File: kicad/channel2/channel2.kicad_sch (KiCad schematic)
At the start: 45 parts, among them J1 Conn_01x07_Male, J5V1 Conn_01x01_Male, Q1 BC846B, Q2 IRF3205, Q3 IRF3205, Q4 BC846B, Q5 IRF3205, Q6 IRF3205, U1 LM324

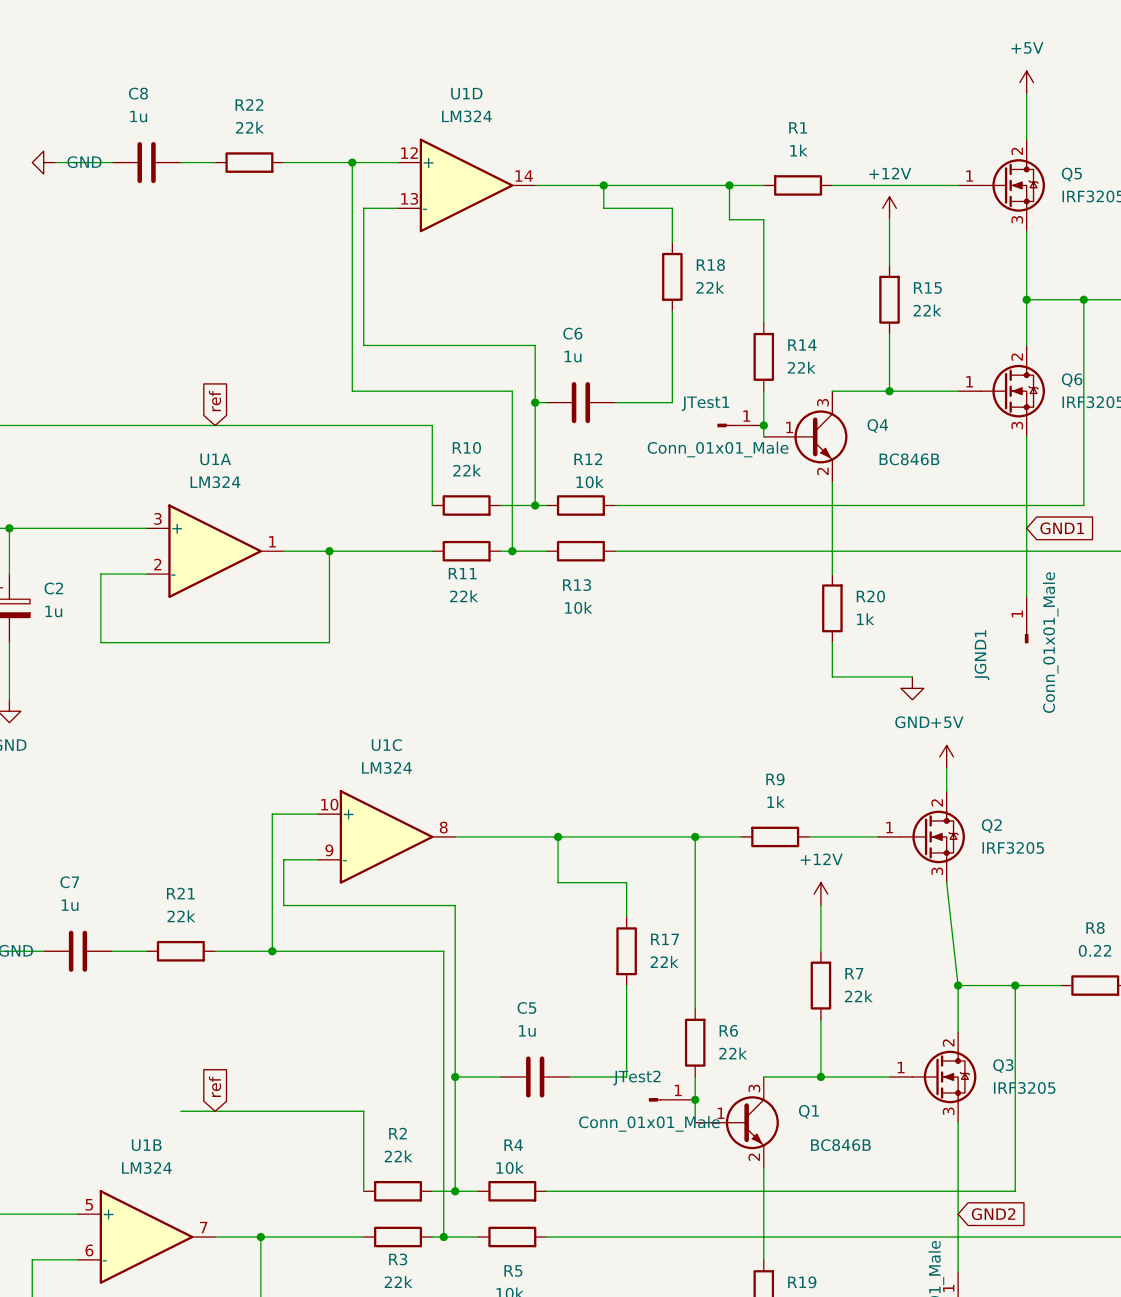
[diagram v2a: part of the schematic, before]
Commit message: minor schematic cleanups, improve opamp compensation
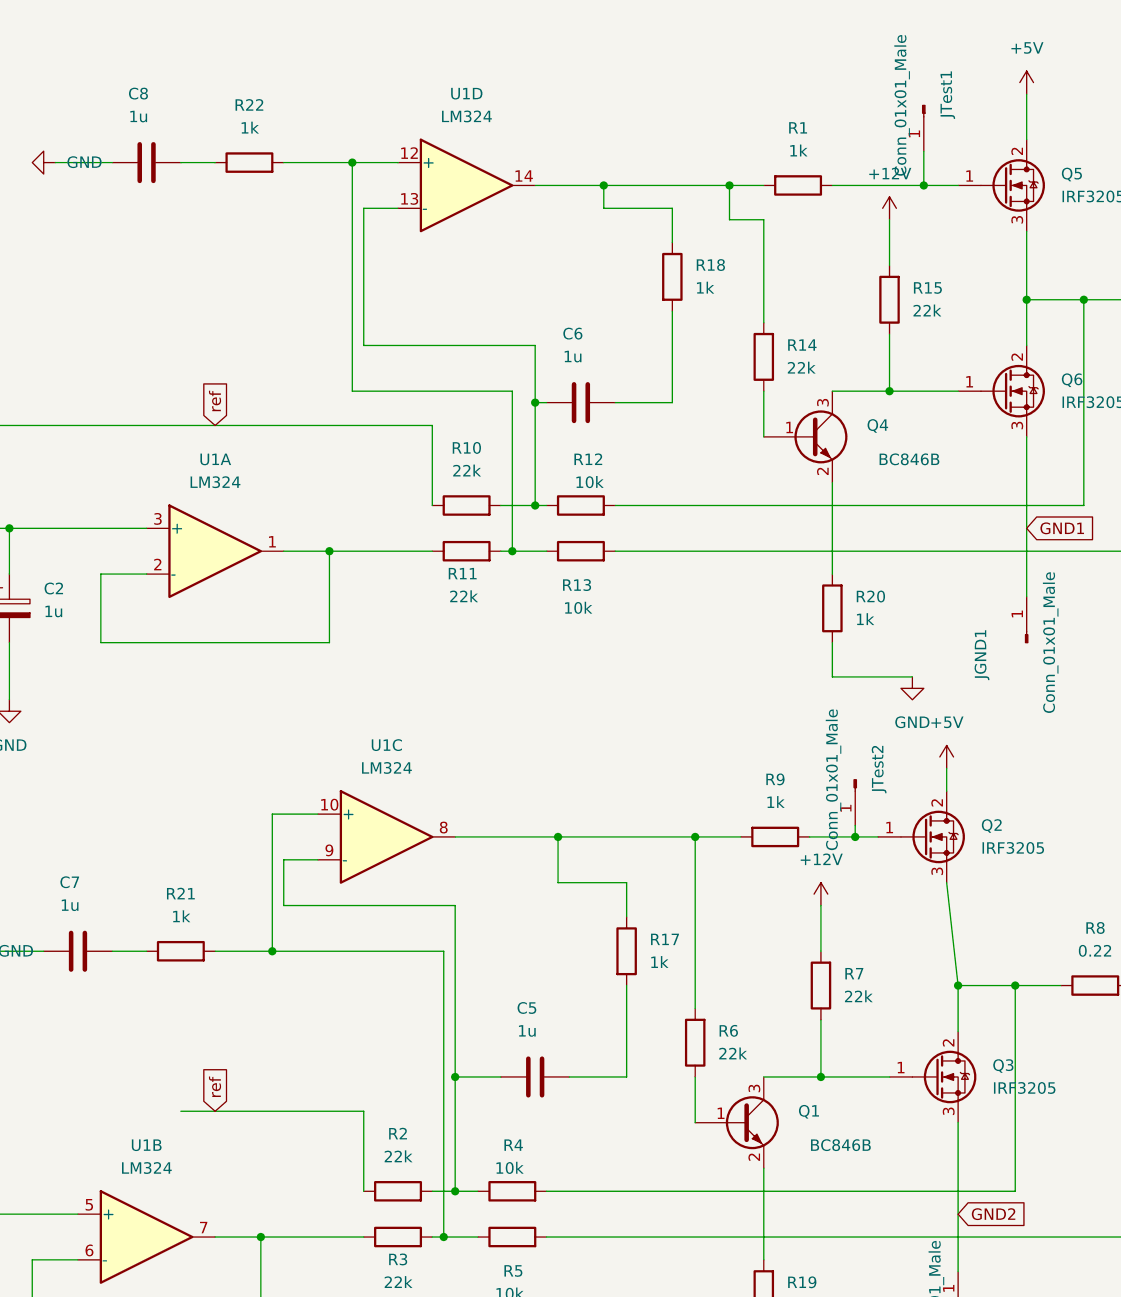
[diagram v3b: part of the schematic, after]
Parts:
- R17, R18, R21, R22: value 22k -> 1k
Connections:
- net at Q5.1 (G), R1.1: now also JTest1.1 (Pin_1)
- net at Q1.1 (B), R6.1: no longer JTest2.1 (Pin_1)
- net at Q2.1 (G), R9.1: now also JTest2.1 (Pin_1)
- net at Q4.1 (B), R14.1: no longer JTest1.1 (Pin_1)
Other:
- moved on the sheet: JTest1, JTest2
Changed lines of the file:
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@@
   (junction (at 232.41 124.46) (diameter 0) (color 0 0 0 0)
   )
+  (junction (at 156.21 105.41) (diameter 0) (color 0 0 0 0)
+  )
   (junction (at 90.17 149.86) (diameter 0) (color 0 0 0 0)
   )
@@
   (junction (at 152.4 132.08) (diameter 0) (color 0 0 0 0)
   )
-  (junction (at 146.05 59.69) (diameter 0) (color 0 0 0 0)
-  )
   (junction (at 167.64 121.92) (diameter 0) (color 0 0 0 0)
   )
@@
   (junction (at 128.27 33.02) (diameter 0) (color 0 0 0 0)
   )
-  (junction (at 138.43 134.62) (diameter 0) (color 0 0 0 0)
-  )
   (junction (at 91.44 118.11) (diameter 0) (color 0 0 0 0)
   )
+  (junction (at 163.83 33.02) (diameter 0) (color 0 0 0 0)
+  )
   (junction (at 100.33 30.48) (diameter 0) (color 0 0 0 0)
   )
@@
     (stroke (width 0) (type default) (color 0 0 0 0))
   )
-  (wire (pts (xy 146.05 55.88) (xy 146.05 59.69))
-    (stroke (width 0) (type default) (color 0 0 0 0))
-  )
   (wire (pts (xy 153.67 66.04) (xy 153.67 76.2))
     (stroke (width 0) (type default) (color 0 0 0 0))
@@
     (stroke (width 0) (type default) (color 0 0 0 0))
   )
-  (wire (pts (xy 138.43 132.08) (xy 138.43 134.62))
-    (stroke (width 0) (type default) (color 0 0 0 0))
-  )
   (wire (pts (xy 123.19 110.49) (xy 130.81 110.49))
     (stroke (width 0) (type default) (color 0 0 0 0))
@@
     (stroke (width 0) (type default) (color 0 0 0 0))
   )
-  (wire (pts (xy 153.67 33.02) (xy 167.64 33.02))
+  (wire (pts (xy 153.67 33.02) (xy 163.83 33.02))
     (stroke (width 0) (type default) (color 0 0 0 0))
   )
@@
     (stroke (width 0) (type default) (color 0 0 0 0))
   )
+  (wire (pts (xy 156.21 104.14) (xy 156.21 105.41))
+    (stroke (width 0) (type default) (color 0 0 0 0))
+  )
   (wire (pts (xy 111.76 132.08) (xy 116.84 132.08))
     (stroke (width 0) (type default) (color 0 0 0 0))
@@
     (stroke (width 0) (type default) (color 0 0 0 0))
   )
+  (wire (pts (xy 163.83 33.02) (xy 167.64 33.02))
+    (stroke (width 0) (type default) (color 0 0 0 0))
+  )
   (wire (pts (xy 152.4 113.03) (xy 152.4 118.11))
     (stroke (width 0) (type default) (color 0 0 0 0))
@@
     (stroke (width 0) (type default) (color 0 0 0 0))
   )
+  (wire (pts (xy 163.83 29.21) (xy 163.83 33.02))
+    (stroke (width 0) (type default) (color 0 0 0 0))
+  )
   (wire (pts (xy 96.52 102.87) (xy 91.44 102.87))
     (stroke (width 0) (type default) (color 0 0 0 0))
@@
     (stroke (width 0) (type default) (color 0 0 0 0))
   )
+  (wire (pts (xy 156.21 105.41) (xy 158.75 105.41))
+    (stroke (width 0) (type default) (color 0 0 0 0))
+  )
   (wire (pts (xy 175.26 45.72) (xy 181.61 45.72))
     (stroke (width 0) (type default) (color 0 0 0 0))
@@
     (stroke (width 0) (type default) (color 0 0 0 0))
   )
-  (wire (pts (xy 138.43 134.62) (xy 138.43 137.16))
+  (wire (pts (xy 138.43 132.08) (xy 138.43 137.16))
     (stroke (width 0) (type default) (color 0 0 0 0))
   )
@@
     (stroke (width 0) (type default) (color 0 0 0 0))
   )
-  (wire (pts (xy 146.05 59.69) (xy 146.05 60.96))
+  (wire (pts (xy 146.05 55.88) (xy 146.05 60.96))
     (stroke (width 0) (type default) (color 0 0 0 0))
   )
@@
     (stroke (width 0) (type default) (color 0 0 0 0))
   )
-  (wire (pts (xy 151.13 105.41) (xy 158.75 105.41))
+  (wire (pts (xy 151.13 105.41) (xy 156.21 105.41))
     (stroke (width 0) (type default) (color 0 0 0 0))
   )
@@
       (effects (font (size 1.27 1.27)) (justify left))
     )
-    (property "Value" "22k" (id 1) (at 133.35 119.3799 0)
+    (property "Value" "1k" (id 1) (at 133.35 119.3799 0)
       (effects (font (size 1.27 1.27)) (justify left))
     )
@@
     (in_bom yes) (on_board yes) (fields_autoplaced)
     (property "Reference" "R21" (id 0) (at 81.28 111.76 90))
-    (property "Value" "22k" (id 1) (at 81.28 114.3 90))
+    (property "Value" "1k" (id 1) (at 81.28 114.3 90))
     (property "Footprint" "Resistor_SMD:R_1206_3216Metric" (id 2) (at 81.28 119.888 90)
       (effects (font (size 1.27 1.27)) hide)
@@
     (in_bom yes) (on_board yes) (fields_autoplaced)
     (property "Reference" "R22" (id 0) (at 88.9 24.13 90))
-    (property "Value" "22k" (id 1) (at 88.9 26.67 90))
+    (property "Value" "1k" (id 1) (at 88.9 26.67 90))
     (property "Footprint" "Resistor_SMD:R_1206_3216Metric" (id 2) (at 88.9 32.258 90)
       (effects (font (size 1.27 1.27)) hide)
@@
       (effects (font (size 1.27 1.27)) (justify left))
     )
-    (property "Value" "22k" (id 1) (at 138.43 44.4499 0)
+    (property "Value" "1k" (id 1) (at 138.43 44.4499 0)
       (effects (font (size 1.27 1.27)) (justify left))
     )
@@
     (pin "2")
   )
-  (symbol (lib_id "Connector:Conn_01x01_Male") (at 133.35 134.62 0) (unit 1)
+  (symbol (lib_id "Connector:Conn_01x01_Male") (at 156.21 99.06 270) (unit 1)
     (in_bom yes) (on_board yes)
-    (property "Reference" "JTest2" (id 0) (at 132.08 132.08 0))
-    (property "Value" "Conn_01x01_Male" (id 1) (at 133.35 137.16 0))
-    (property "Footprint" "Connector_PinHeader_2.54mm:PinHeader_1x01_P2.54mm_Vertical" (id 2) (at 133.35 134.62 0)
-      (effects (font (size 1.27 1.27)) hide)
-    )
-    (property "Datasheet" "~" (id 3) (at 133.35 134.62 0)
+    (property "Reference" "JTest2" (id 0) (at 158.75 97.79 0))
+    (property "Value" "Conn_01x01_Male" (id 1) (at 153.67 99.06 0))
+    (property "Footprint" "Connector_PinHeader_2.54mm:PinHeader_1x01_P2.54mm_Vertical" (id 2) (at 156.21 99.06 0)
+      (effects (font (size 1.27 1.27)) hide)
+    )
+    (property "Datasheet" "~" (id 3) (at 156.21 99.06 0)
       (effects (font (size 1.27 1.27)) hide)
     )
@@
     (pin "2")
   )
-  (symbol (lib_id "Connector:Conn_01x01_Male") (at 140.97 59.69 0) (unit 1)
+  (symbol (lib_id "Connector:Conn_01x01_Male") (at 163.83 24.13 270) (unit 1)
     (in_bom yes) (on_board yes)
-    (property "Reference" "JTest1" (id 0) (at 139.7 57.15 0))
-    (property "Value" "Conn_01x01_Male" (id 1) (at 140.97 62.23 0))
-    (property "Footprint" "Connector_PinHeader_2.54mm:PinHeader_1x01_P2.54mm_Vertical" (id 2) (at 140.97 59.69 0)
-      (effects (font (size 1.27 1.27)) hide)
-    )
-    (property "Datasheet" "~" (id 3) (at 140.97 59.69 0)
+    (property "Reference" "JTest1" (id 0) (at 166.37 22.86 0))
+    (property "Value" "Conn_01x01_Male" (id 1) (at 161.29 24.13 0))
+    (property "Footprint" "Connector_PinHeader_2.54mm:PinHeader_1x01_P2.54mm_Vertical" (id 2) (at 163.83 24.13 0)
+      (effects (font (size 1.27 1.27)) hide)
+    )
+    (property "Datasheet" "~" (id 3) (at 163.83 24.13 0)
       (effects (font (size 1.27 1.27)) hide)
     )
@@
     )
     (path "/01714dbf-5482-49df-a970-7f8af8ba7fd9"
-      (reference "R17") (unit 1) (value "22k") (footprint "Resistor_SMD:R_1206_3216Metric")
+      (reference "R17") (unit 1) (value "1k") (footprint "Resistor_SMD:R_1206_3216Metric")
     )
     (path "/74a2f18b-7a4d-48b7-bae8-39cebb1c68ea"
-      (reference "R18") (unit 1) (value "22k") (footprint "Resistor_SMD:R_1206_3216Metric")
+      (reference "R18") (unit 1) (value "1k") (footprint "Resistor_SMD:R_1206_3216Metric")
     )
     (path "/2d1ea026-a64f-45f8-b9b5-9a0b3db75686"
@@
     )
     (path "/29179f6f-ac0f-419e-9644-3e7dc970e2a3"
-      (reference "R21") (unit 1) (value "22k") (footprint "Resistor_SMD:R_1206_3216Metric")
+      (reference "R21") (unit 1) (value "1k") (footprint "Resistor_SMD:R_1206_3216Metric")
     )
     (path "/4d774a5a-607a-4d29-9f94-c363465187d2"
-      (reference "R22") (unit 1) (value "22k") (footprint "Resistor_SMD:R_1206_3216Metric")
+      (reference "R22") (unit 1) (value "1k") (footprint "Resistor_SMD:R_1206_3216Metric")
     )
     (path "/e72258c2-989b-417f-a235-afe35cbb8e8d"
